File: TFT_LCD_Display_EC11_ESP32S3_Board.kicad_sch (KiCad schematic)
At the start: 44 parts, among them J1 MOLEX-503398-1892, J2 USB_C_Receptacle_USB2.0_16P, J3 I2C, J4 POWER, J5 SPARE, J6 TFT-LCD-DISPLAY-EC11, SW1 BOOT, SW2 EN, U1 MCP1826S, U2 ESP32-S3-WROOM-1

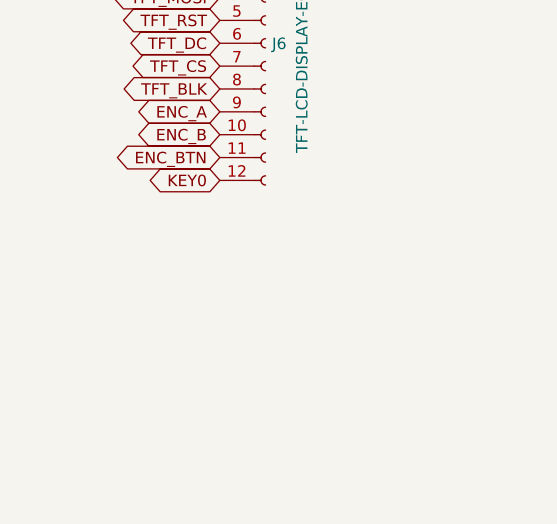
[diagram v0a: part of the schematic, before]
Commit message: r3.1 - Orientation D1 was wrong
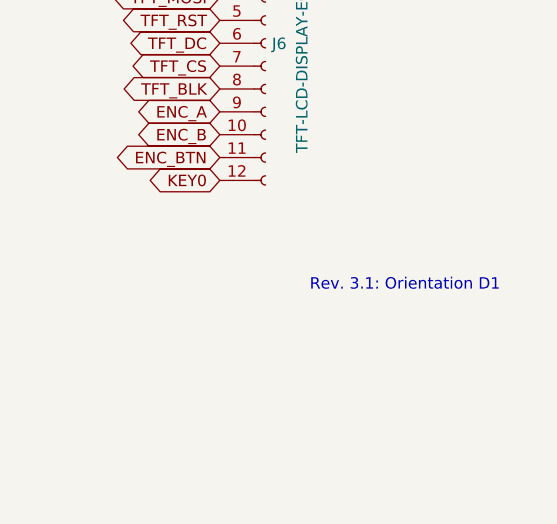
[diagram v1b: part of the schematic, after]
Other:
- note added: "Rev. 3.1: Orientation D1"

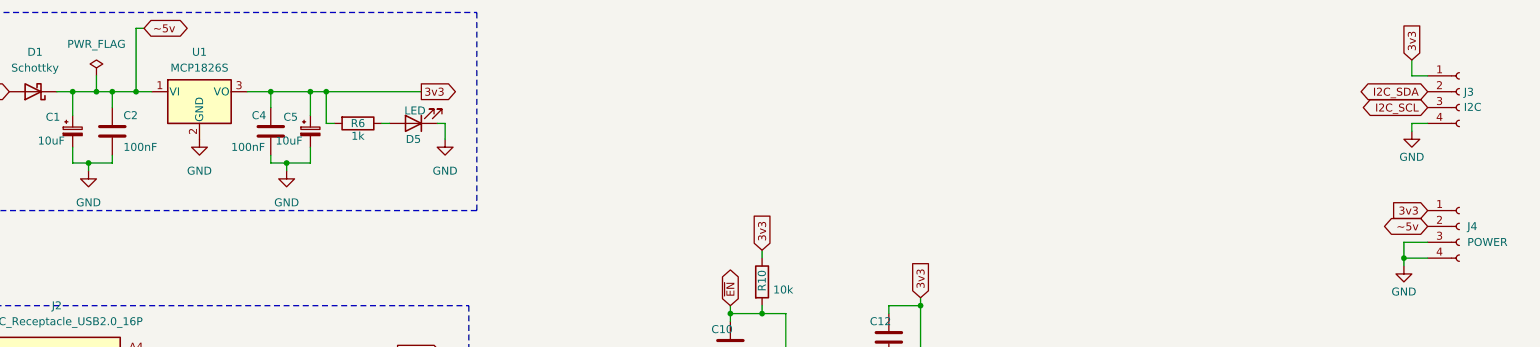
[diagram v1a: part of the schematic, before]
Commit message: J4 ~5v now is real VBUS 5v
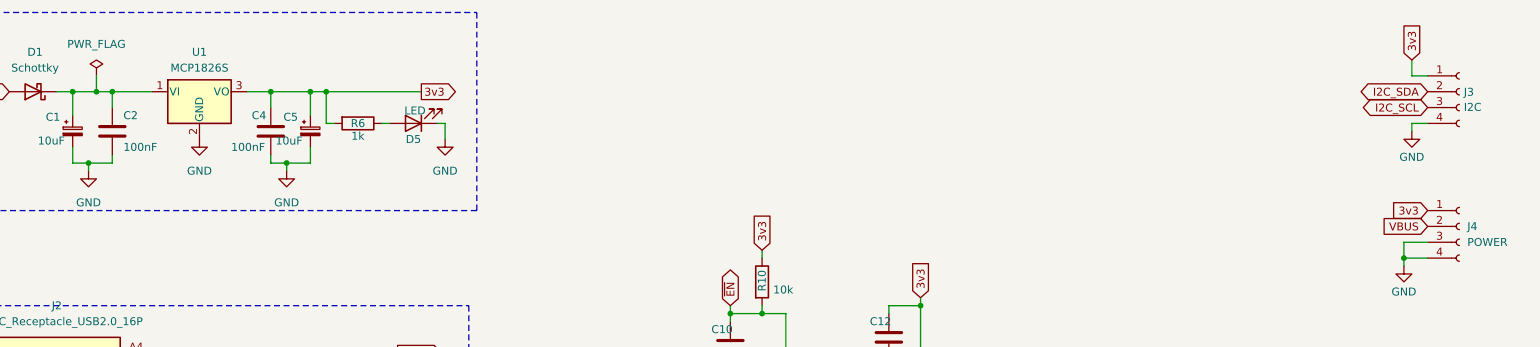
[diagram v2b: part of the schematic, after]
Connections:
- net VBUS: now also J4.2 (Pin_2)
- net ~5v: no longer names the net of C1.1, C2.1, D1.1 (K), U1.1 (VI)
- net ~5v: no longer J4.2 (Pin_2)
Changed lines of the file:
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@@
-	)
-	(junction
-		(at 46.99 27.94)
-		(diameter 0)
-		(color 0 0 0 0)
 	)
 	(junction
@@
 	(wire
 		(pts
-			(xy 43.18 27.94) (xy 46.99 27.94)
+			(xy 43.18 27.94) (xy 49.53 27.94)
 		)
 		(stroke
@@
 	(wire
 		(pts
-			(xy 48.26 17.78) (xy 46.99 17.78)
-		)
-		(stroke
-			(width 0)
-			(type default)
-		)
-	)
-	(wire
-		(pts
 			(xy 39.37 39.37) (xy 43.18 39.37)
 		)
@@
 	(wire
 		(pts
-			(xy 46.99 27.94) (xy 49.53 27.94)
-		)
-		(stroke
-			(width 0)
-			(type default)
-		)
-	)
-	(wire
-		(pts
 			(xy 50.8 87.63) (xy 50.8 88.9)
 		)
@@
 		(pts
 			(xy 135.89 172.72) (xy 135.89 173.99)
-		)
-		(stroke
-			(width 0)
-			(type default)
-		)
-	)
-	(wire
-		(pts
-			(xy 46.99 17.78) (xy 46.99 27.94)
 		)
 		(stroke
@@
 		)
 	)
-	(global_label "~5v"
-		(shape bidirectional)
+	(global_label "VBUS"
+		(shape input)
 		(at 254 49.53 180)
 		(fields_autoplaced yes)
@@
 		)
 		(property "Intersheetrefs" "${INTERSHEET_REFS}"
-			(at 246.8193 49.53 0)
+			(at 246.1162 49.53 0)
 			(hide yes)
 			(show_name no)
@@
 			)
 		)
-	)
-	(global_label "~5v"
-		(shape bidirectional)
-		(at 48.26 17.78 0)
-		(fields_autoplaced yes)
-		(effects
-			(font
-				(size 1.27 1.27)
-			)
-			(justify left)
-		)
-		(property "Intersheetrefs" "${INTERSHEET_REFS}"
-			(at 55.4407 17.78 0)
-			(hide yes)
-			(show_name no)
-			(do_not_autoplace no)
-			(effects
-				(font
-					(size 1.27 1.27)
-				)
-				(justify left)
-			)
-		)
